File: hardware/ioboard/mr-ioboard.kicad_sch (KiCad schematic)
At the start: 115 parts, among them J1 Conn_01x40_Shielded, J2 USB_C_Receptacle_USB2.0, J3 Conn_01x06, J4 Micro_SD_Card_Det, J5 Conn_01x04, Q1 2N7002, SW1 SW_Push, U1 TPS62822, U10 F1C200S, U2 TPS56637, U3 TPD2E2U06, U4 DS90C363, U5 TPD2E2U06, U6 LD3985M28R_SOT23, U7 TPS62822, U8 FUSB302BMPX, U9 TPD2E2U06, Y1 24MHz

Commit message: Initial IO board layout
Signed-off-by: gatecat <gatecat@ds0.me>
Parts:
- C21: footprint Capacitor_SMD:C_0805_2012Metric -> Capacitor_SMD:C_0402_1005Metric
- J4: footprint (none) -> Connector_Card:microSD_HC_Hirose_DM3BT-DSF-PEJS
- RN1, RN2, RN3, RN4: footprint Resistor_SMD:R_0402_1005Metric -> Resistor_SMD:R_Array_Convex_4x0402
- U3, U5, U9: footprint Package_TO_SOT_SMD:SOT-543 -> Package_TO_SOT_SMD:SOT-553
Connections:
- net GND: now also C34.2, C36.2, C43.2, C47.2
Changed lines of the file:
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@@
   (junction (at 374.65 90.17) (diameter 1.016) (color 0 0 0 0))
   (junction (at 375.92 46.99) (diameter 1.016) (color 0 0 0 0))
+  (junction (at 377.19 71.12) (diameter 1.016) (color 0 0 0 0))
   (junction (at 378.46 181.61) (diameter 1.016) (color 0 0 0 0))
   (junction (at 378.46 191.77) (diameter 1.016) (color 0 0 0 0))
@@
     (stroke (width 0) (type solid) (color 0 0 0 0))
   )
+  (wire (pts (xy 377.19 71.12) (xy 383.54 71.12))
+    (stroke (width 0) (type solid) (color 0 0 0 0))
+  )
   (wire (pts (xy 378.46 181.61) (xy 378.46 173.99))
     (stroke (width 0) (type solid) (color 0 0 0 0))
@@
     (pin "1")
   )
+  (symbol (lib_id "power:GND") (at 383.54 71.12 90) (unit 1)
+    (in_bom yes) (on_board yes)
+    (property "Reference" "#PWR?" (id 0) (at 389.89 71.12 0)
+      (effects (font (size 1.27 1.27)) hide)
+    )
+    (property "Value" "GND" (id 1) (at 386.7151 71.0057 90)
+      (effects (font (size 1.27 1.27)) (justify right))
+    )
+    (property "Footprint" "" (id 2) (at 383.54 71.12 0)
+      (effects (font (size 1.27 1.27)) hide)
+    )
+    (property "Datasheet" "" (id 3) (at 383.54 71.12 0)
+      (effects (font (size 1.27 1.27)) hide)
+    )
+    (pin "1")
+  )
   (symbol (lib_id "power:GND") (at 387.35 162.56 0) (unit 1)
     (in_bom yes) (on_board yes)
@@
       (effects (font (size 1.27 1.27)) (justify left))
     )
-    (property "Footprint" "Capacitor_SMD:C_0805_2012Metric" (id 2) (at 175.26 39.37 0)
+    (property "Footprint" "Capacitor_SMD:C_0402_1005Metric" (id 2) (at 175.26 39.37 0)
       (effects (font (size 1.27 1.27)) hide)
     )
@@
       (effects (font (size 1.27 1.27)) (justify left))
     )
-    (property "Footprint" "Resistor_SMD:R_0402_1005Metric" (id 2) (at 156.845 233.68 90)
+    (property "Footprint" "Resistor_SMD:R_Array_Convex_4x0402" (id 2) (at 156.845 233.68 90)
       (effects (font (size 1.27 1.27)) hide)
     )
@@
       (effects (font (size 1.27 1.27)) (justify left))
     )
-    (property "Footprint" "Resistor_SMD:R_0402_1005Metric" (id 2) (at 177.165 233.68 90)
+    (property "Footprint" "Resistor_SMD:R_Array_Convex_4x0402" (id 2) (at 177.165 233.68 90)
       (effects (font (size 1.27 1.27)) hide)
     )
@@
       (effects (font (size 1.27 1.27)) (justify left))
     )
-    (property "Footprint" "Resistor_SMD:R_0402_1005Metric" (id 2) (at 207.645 128.27 90)
+    (property "Footprint" "Resistor_SMD:R_Array_Convex_4x0402" (id 2) (at 207.645 128.27 90)
       (effects (font (size 1.27 1.27)) hide)
     )
@@
       (effects (font (size 1.27 1.27)) (justify left))
     )
-    (property "Footprint" "Resistor_SMD:R_0402_1005Metric" (id 2) (at 217.805 128.27 90)
+    (property "Footprint" "Resistor_SMD:R_Array_Convex_4x0402" (id 2) (at 217.805 128.27 90)
       (effects (font (size 1.27 1.27)) hide)
     )
@@
     (property "Reference" "U3" (id 0) (at 83.82 257.4098 0))
     (property "Value" "TPD2E2U06" (id 1) (at 83.82 259.7085 0))
-    (property "Footprint" "Package_TO_SOT_SMD:SOT-543" (id 2) (at 63.5 273.05 0)
+    (property "Footprint" "Package_TO_SOT_SMD:SOT-553" (id 2) (at 63.5 273.05 0)
       (effects (font (size 1.27 1.27)) hide)
     )
@@
     (property "Reference" "U5" (id 0) (at 105.41 257.4098 0))
     (property "Value" "TPD2E2U06" (id 1) (at 105.41 259.7085 0))
-    (property "Footprint" "Package_TO_SOT_SMD:SOT-543" (id 2) (at 85.09 273.05 0)
+    (property "Footprint" "Package_TO_SOT_SMD:SOT-553" (id 2) (at 85.09 273.05 0)
       (effects (font (size 1.27 1.27)) hide)
     )
@@
     (property "Reference" "U9" (id 0) (at 251.46 210.4198 0))
     (property "Value" "TPD2E2U06" (id 1) (at 251.46 212.7185 0))
-    (property "Footprint" "Package_TO_SOT_SMD:SOT-543" (id 2) (at 231.14 226.06 0)
+    (property "Footprint" "Package_TO_SOT_SMD:SOT-553" (id 2) (at 231.14 226.06 0)
       (effects (font (size 1.27 1.27)) hide)
     )
@@
     (property "Reference" "J4" (id 0) (at 204.47 239.6298 0))
     (property "Value" "Micro_SD_Card_Det" (id 1) (at 204.47 241.9285 0))
-    (property "Footprint" "" (id 2) (at 257.81 242.57 0)
+    (property "Footprint" "Connector_Card:microSD_HC_Hirose_DM3BT-DSF-PEJS" (id 2) (at 257.81 242.57 0)
       (effects (font (size 1.27 1.27)) hide)
     )
@@
       (reference "#PWR0166") (unit 1) (value "+3V3") (footprint "")
     )
+    (path "/1cda516c-3e6f-4ad0-9879-0136f4e32e6b"
+      (reference "#PWR?") (unit 1) (value "GND") (footprint "")
+    )
     (path "/f9888b35-f80f-493e-bc0c-cacecf49daf2"
       (reference "AE1") (unit 1) (value "Antenna_Chip") (footprint "RF_Antenna:Johanson_2450AT43F0100")
@@
     )
     (path "/62e423d8-332e-4d8c-925a-b0da77dcc1cf"
-      (reference "C21") (unit 1) (value "10n") (footprint "Capacitor_SMD:C_0805_2012Metric")
+      (reference "C21") (unit 1) (value "10n") (footprint "Capacitor_SMD:C_0402_1005Metric")
     )
     (path "/f2a743dc-3c5d-406d-be9b-3c0dda479c62"
@@
     )
     (path "/01f19cac-f2a9-419a-a0e2-5088a25bddf3"
-      (reference "J4") (unit 1) (value "Micro_SD_Card_Det") (footprint "")
+      (reference "J4") (unit 1) (value "Micro_SD_Card_Det") (footprint "Connector_Card:microSD_HC_Hirose_DM3BT-DSF-PEJS")
     )
     (path "/49eb76a8-7033-41e7-9d48-fde1ab72fc35"
@@
     )
     (path "/11d70e8a-d389-41cc-a0fa-66e675dc5cc4"
-      (reference "RN1") (unit 1) (value "47k") (footprint "Resistor_SMD:R_0402_1005Metric")
+      (reference "RN1") (unit 1) (value "47k") (footprint "Resistor_SMD:R_Array_Convex_4x0402")
     )
     (path "/175feb45-f987-4cf9-996e-3044207fc889"
-      (reference "RN2") (unit 1) (value "47k") (footprint "Resistor_SMD:R_0402_1005Metric")
+      (reference "RN2") (unit 1) (value "47k") (footprint "Resistor_SMD:R_Array_Convex_4x0402")
     )
     (path "/acb52a5e-0922-4adc-a1ae-4c3e6fffbdad"
-      (reference "RN3") (unit 1) (value "47k") (footprint "Resistor_SMD:R_0402_1005Metric")
+      (reference "RN3") (unit 1) (value "47k") (footprint "Resistor_SMD:R_Array_Convex_4x0402")
     )
     (path "/08ce3bcc-d331-4362-bb52-d1b9b39488f7"
-      (reference "RN4") (unit 1) (value "47k") (footprint "Resistor_SMD:R_0402_1005Metric")
+      (reference "RN4") (unit 1) (value "47k") (footprint "Resistor_SMD:R_Array_Convex_4x0402")
     )
     (path "/72e45b81-c1c3-4f34-bbf4-ae3166fb09d8"
@@
     )
     (path "/53d12aea-c49c-4c1b-b028-be0c53dc30ce"
-      (reference "U3") (unit 1) (value "TPD2E2U06") (footprint "Package_TO_SOT_SMD:SOT-543")
+      (reference "U3") (unit 1) (value "TPD2E2U06") (footprint "Package_TO_SOT_SMD:SOT-553")
     )
     (path "/5c255aa5-0e1c-4fda-8a72-9577d822c847"
@@
     )
     (path "/123e626b-fdd0-4622-9f4f-1211d3c21d18"
-      (reference "U5") (unit 1) (value "TPD2E2U06") (footprint "Package_TO_SOT_SMD:SOT-543")
+      (reference "U5") (unit 1) (value "TPD2E2U06") (footprint "Package_TO_SOT_SMD:SOT-553")
     )
     (path "/355b7f35-b2ba-4061-80db-d4e64dbf1194"
@@
     )
     (path "/5a5b54a3-8111-4063-843e-decc7b4de43f"
-      (reference "U9") (unit 1) (value "TPD2E2U06") (footprint "Package_TO_SOT_SMD:SOT-543")
+      (reference "U9") (unit 1) (value "TPD2E2U06") (footprint "Package_TO_SOT_SMD:SOT-553")
     )
     (path "/86a39066-7989-449a-90f9-ad2b9221de0b"

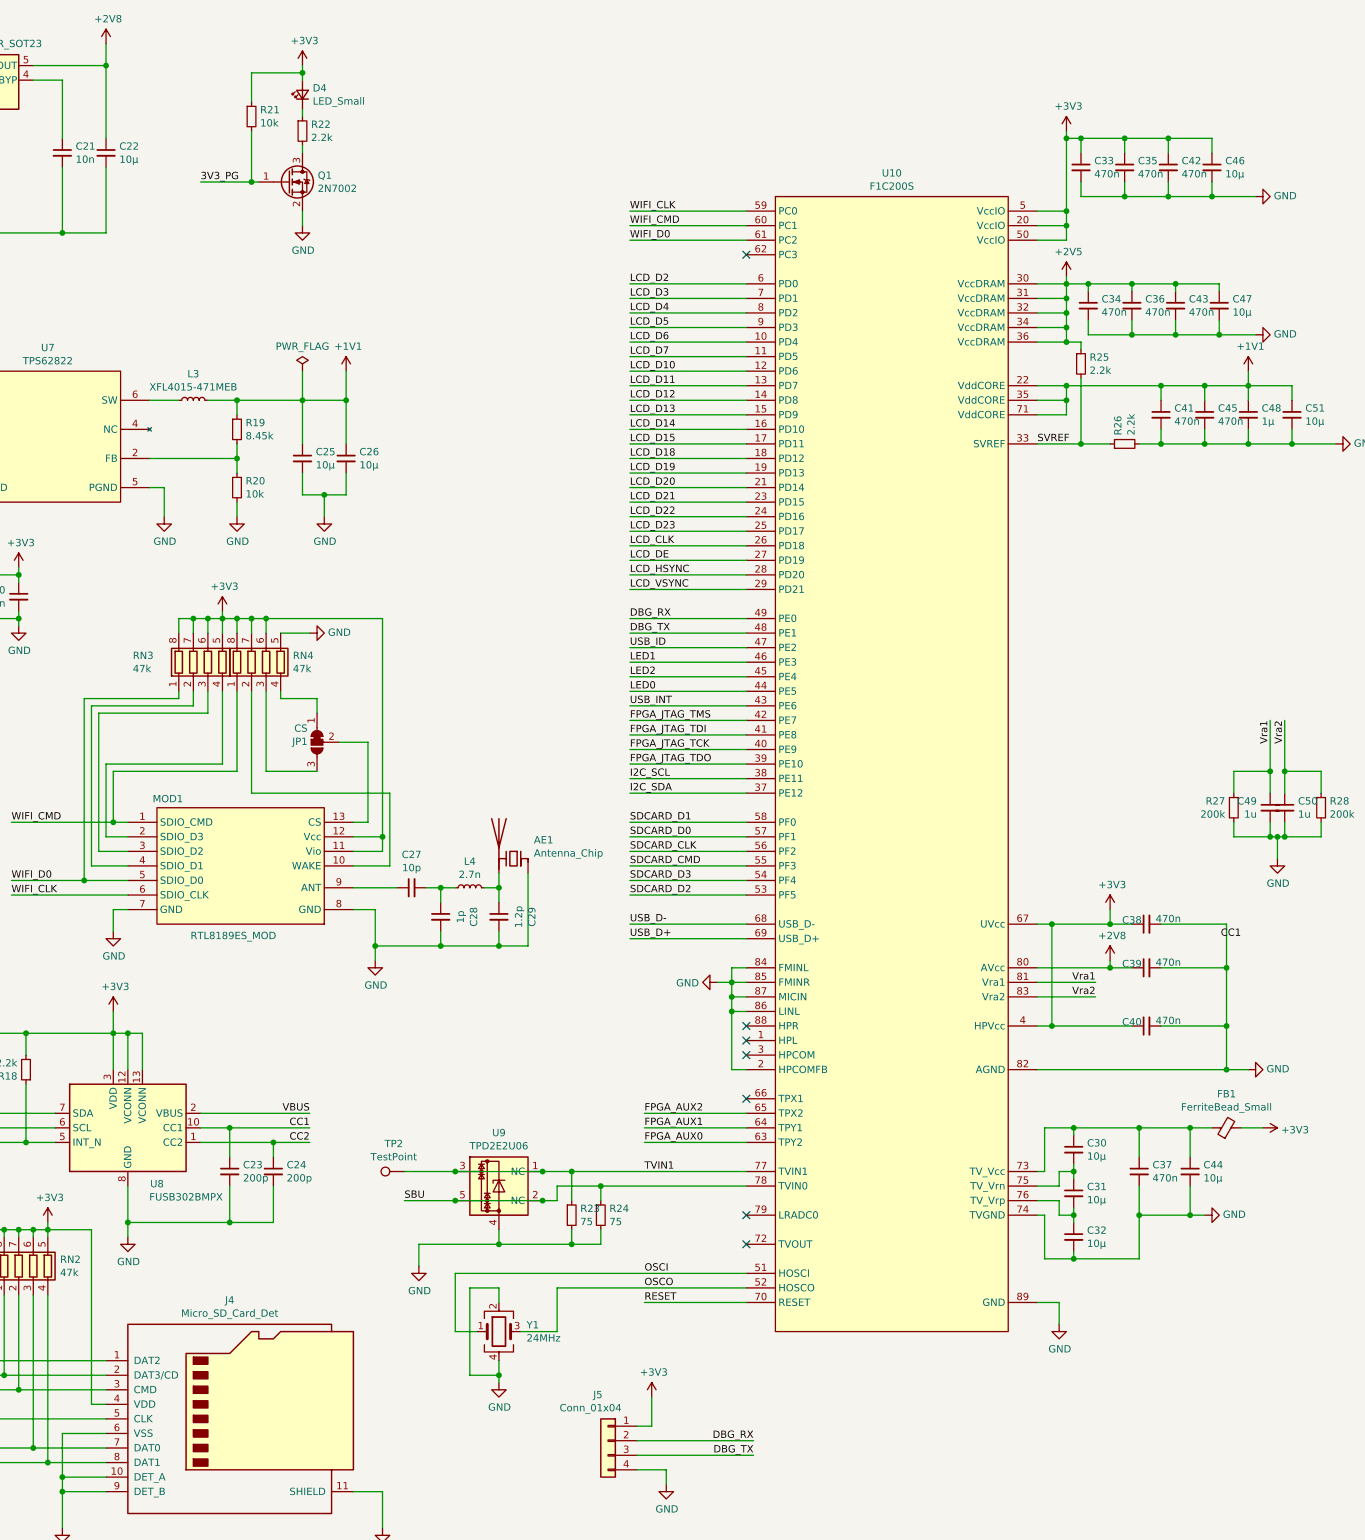
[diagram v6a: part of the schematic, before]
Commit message: Add a few missing parts to IO board
Signed-off-by: gatecat <gatecat@ds0.me>
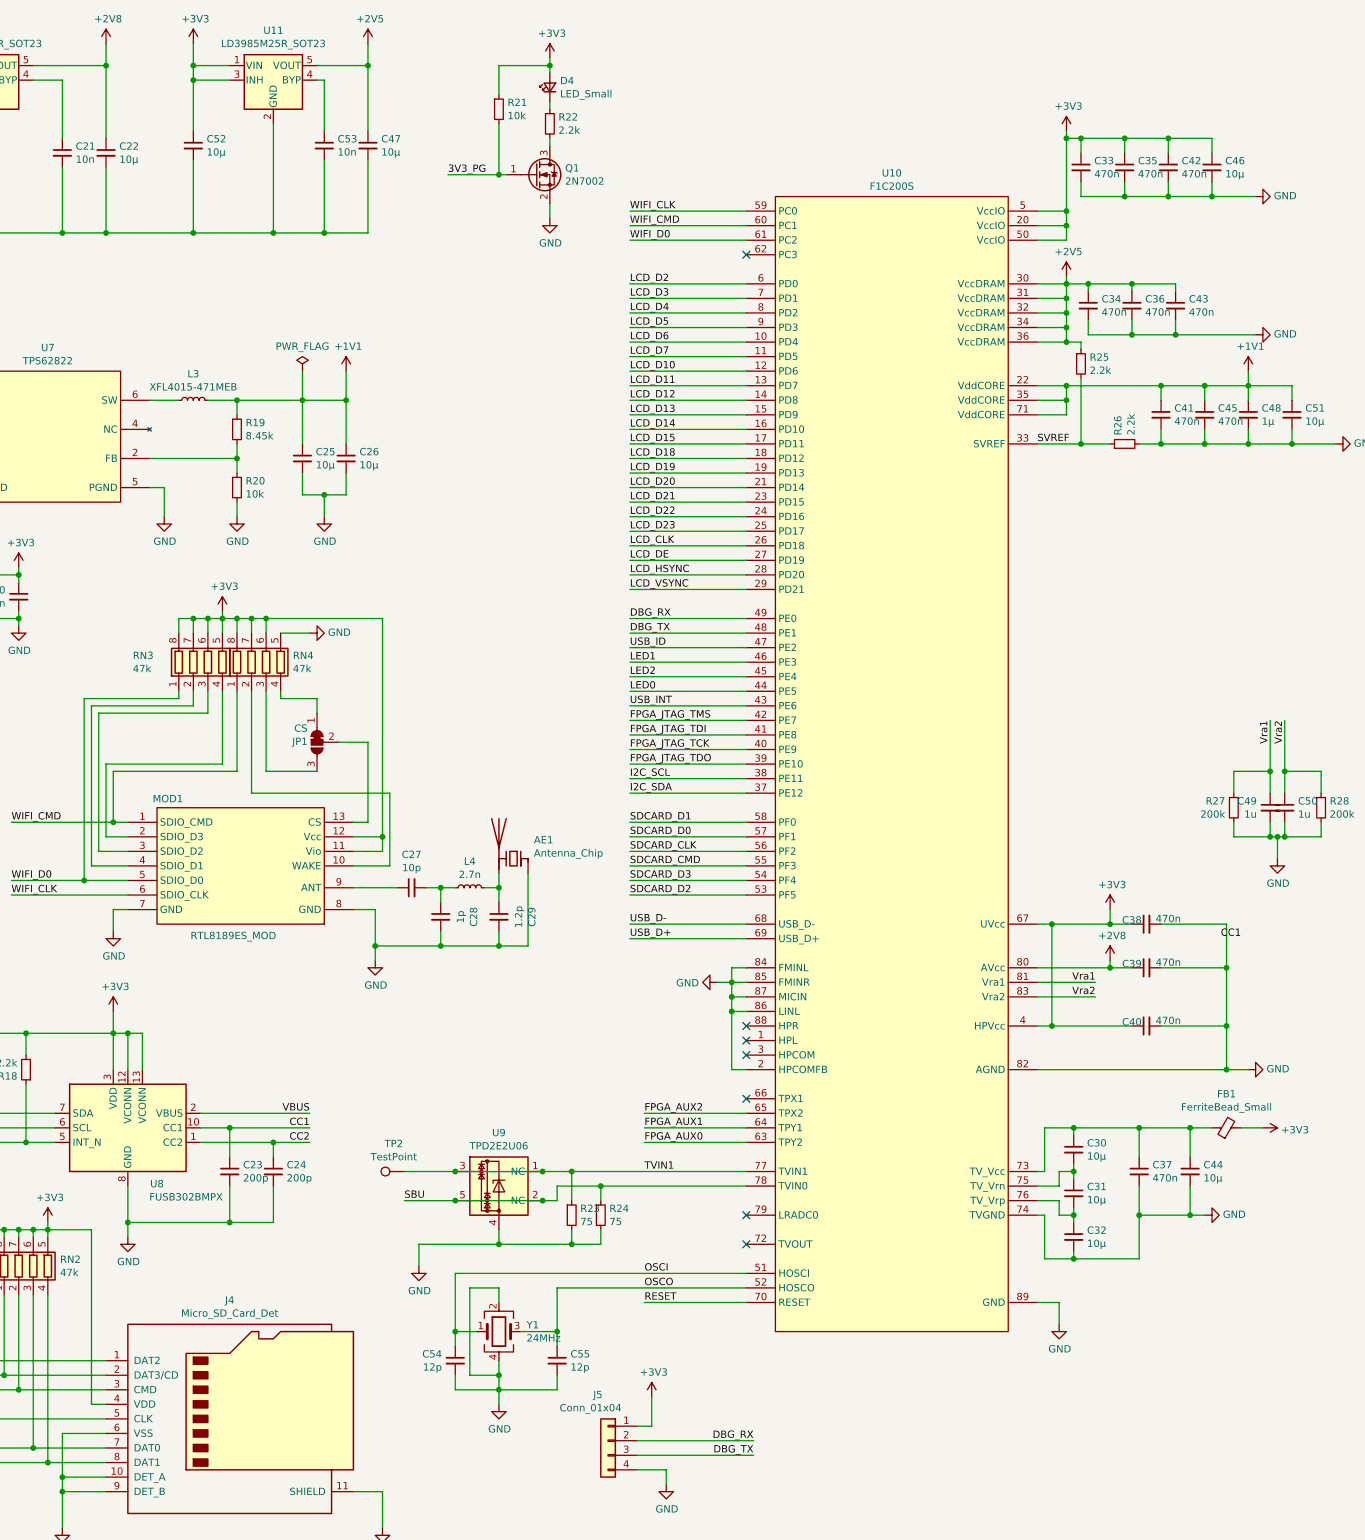
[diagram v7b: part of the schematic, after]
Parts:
- added C52: 10µ, Capacitor_SMD:C_0805_2012Metric, symbol Device:C_Small
- added C53: 10n, Capacitor_SMD:C_0402_1005Metric, symbol Device:C_Small
- added C54, C55: 12p, symbol Device:C_Small
- added U11: LD3985M25R_SOT23, Package_TO_SOT_SMD:SOT-23-5, symbol Regulator_Linear:LD3985M25R_SOT23
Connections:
- net +2V5: now also U11.5 (VOUT)
- net +3V3: now also C52.1, U11.1 (VIN), U11.3 (INH)
- net GND: now also C52.2, C53.2, C54.2, C55.2, U11.2 (GND)
- net OSCI: now also C54.1
- net OSCO: now also C55.1
- new net: C53.1, U11.4 (BYP)
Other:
- moved on the sheet: C47, D4, Q1, R21, R22

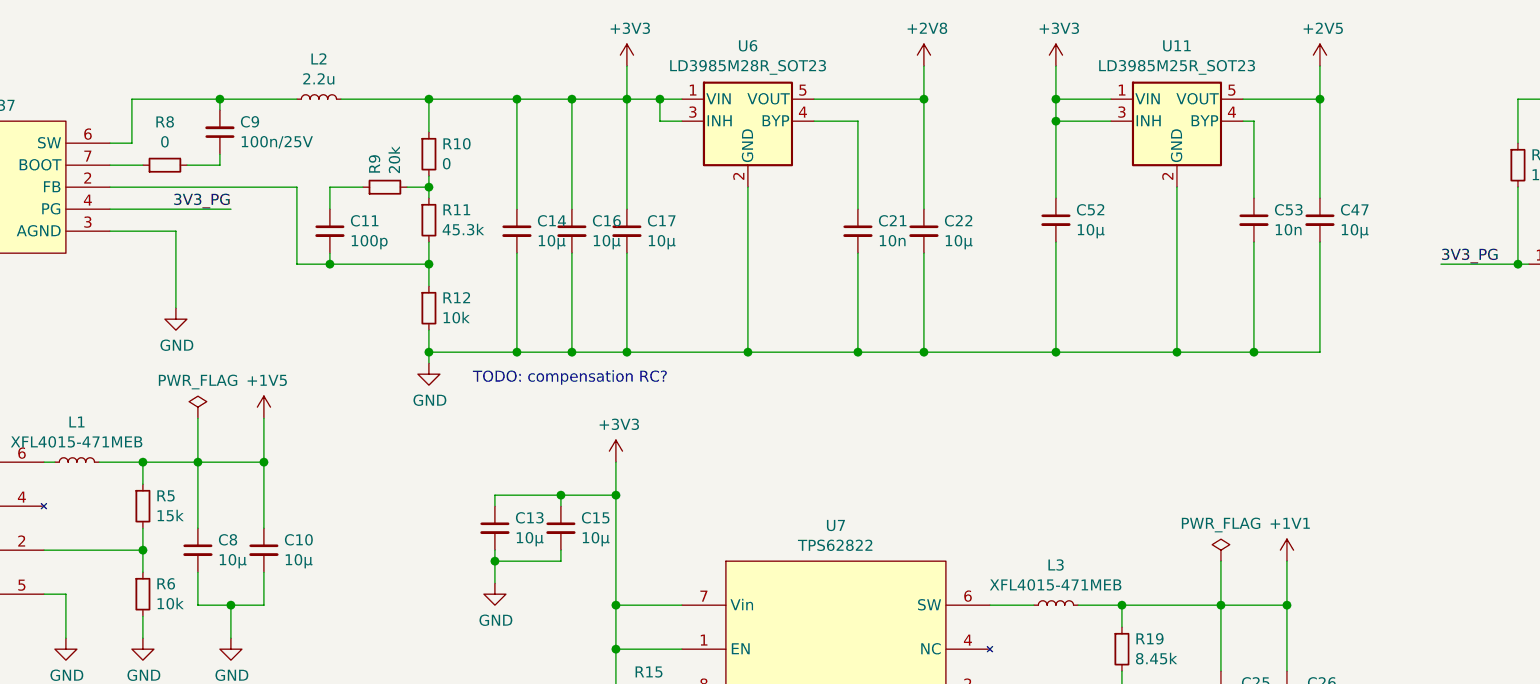
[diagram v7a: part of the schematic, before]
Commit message: Fix IO board 2.5V supply
Signed-off-by: gatecat <gatecat@ds0.me>
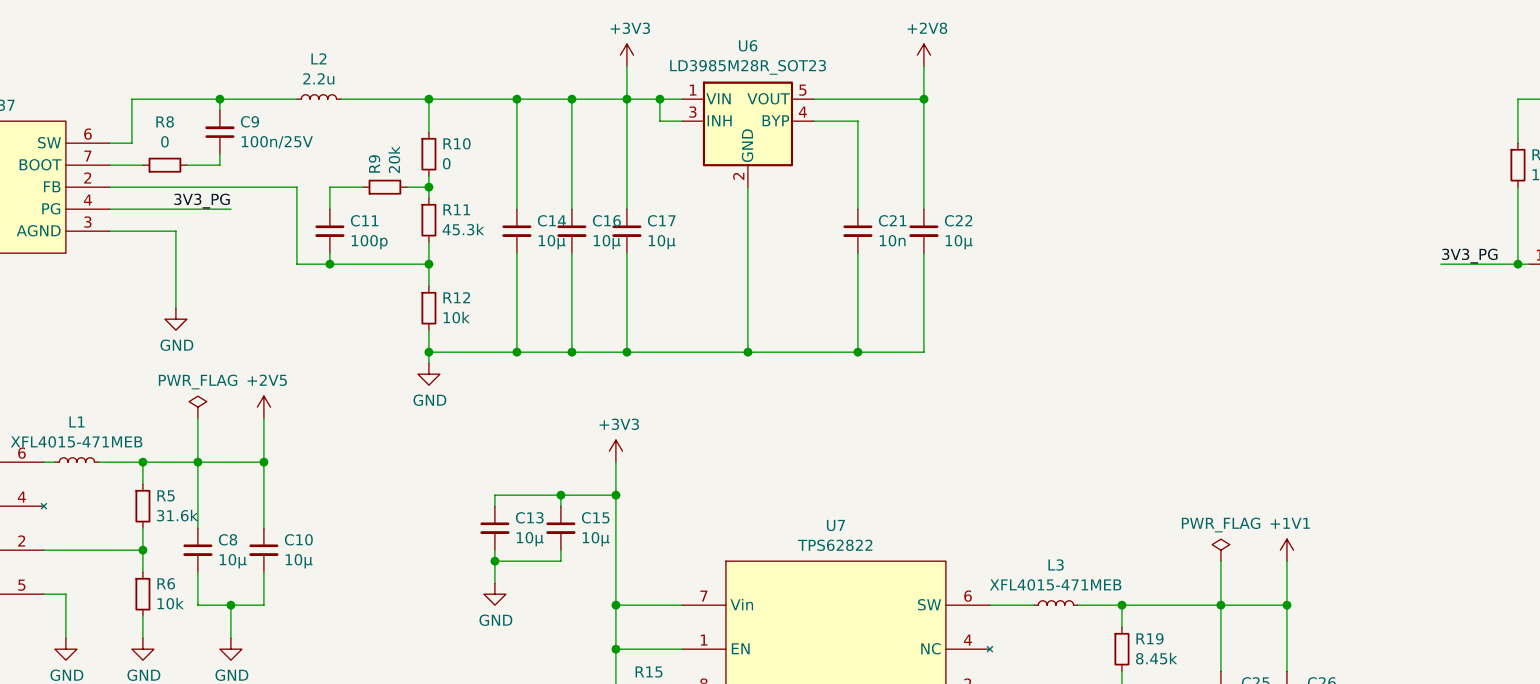
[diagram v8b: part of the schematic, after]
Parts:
- removed C47, C52: 10µ, Capacitor_SMD:C_0805_2012Metric, symbol Device:C_Small
- removed C53: 10n, Capacitor_SMD:C_0402_1005Metric, symbol Device:C_Small
- removed U11: LD3985M25R_SOT23, Package_TO_SOT_SMD:SOT-23-5, symbol Regulator_Linear:LD3985M25R_SOT23
- R5: value 15k -> 31.6k
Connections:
- net +1V5 is gone; now on net +2V5: C10.1, C8.1, L1.2, R5.1
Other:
- note removed: "TODO: compensation RC?"
